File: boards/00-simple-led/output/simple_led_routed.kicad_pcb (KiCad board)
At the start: 2 copper layers, 25 x 20 mm, 3 parts, among them J1 PWR

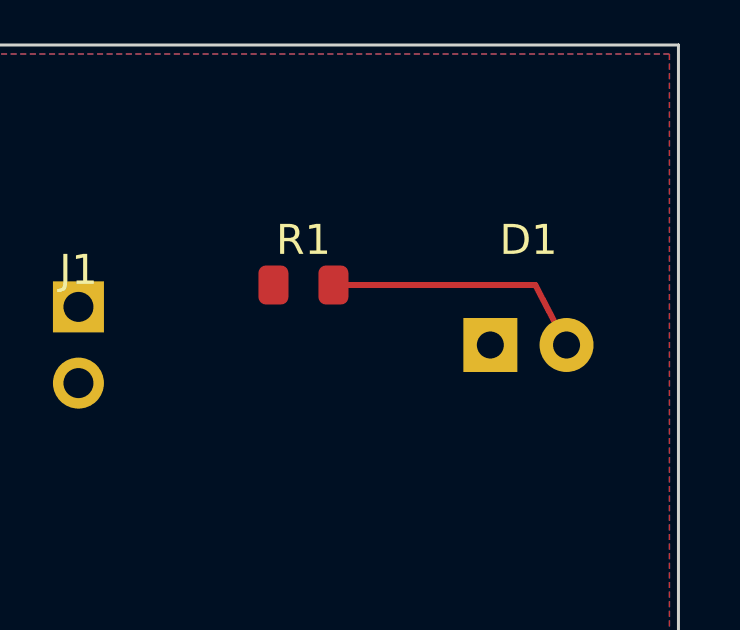
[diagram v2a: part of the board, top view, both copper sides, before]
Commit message: fix(board-00): true-45 LED_ANODE knee so the descent clears the 45° census gate
The GND-clearance guard in _rewrite_led_anode_route() nudged the knee to
(d1_gnd_x + 1.5, ...), giving the descent leg unequal dx/dy (1.04/2.0) =
62.53°, which fails the #3532 45°-alignment census gate
(test_fleet_45_census). Replace the off-45 nudge with a true-45 knee
(dx == dy, placed abs(dy) west of the anode); since the diagonal runs
south-east toward the anode it moves away from D1's GND pad (1.8mm
clearance), so no nudge is needed. Keep a 45-preserving safety fallback
(due-north 90° descent) for future footprint changes — never an off-45
nudge. Regenerate routed PCB + jlcpcb-tier1 manufacturing bundle.

Board 00 stays 0 under both DRC engines, LED_ANODE still connects
R1.2 → D1.2 (ANODE, not GND), diff is board-local.

Co-Authored-By: Claude Opus 4.7 <noreply@anthropic.com>
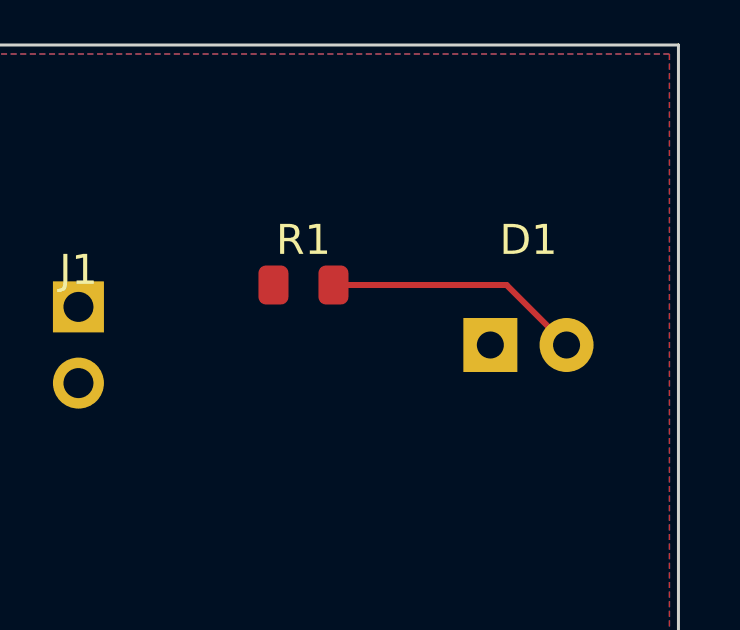
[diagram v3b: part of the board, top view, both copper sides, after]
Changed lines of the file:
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@@
 	(net 2 "LED_ANODE")
 	(net 3 "GND")
+	(footprint "Connector_PinHeader_2.54mm:PinHeader_1x02_P2.54mm_Vertical"
+		(layer "F.Cu")
+		(at 105 110)
+		(property "Reference" "J1"
+			(at 0 -2.5 0)
+			(layer "F.SilkS")
+			(effects
+				(font
+					(size 1 1)
+					(thickness 0.15)
+				)
+			)
+		)
+		(property "Value" "PWR"
+			(at 0 4 0)
+			(layer "F.Fab")
+			(effects
+				(font
+					(size 1 1)
+					(thickness 0.15)
+				)
+			)
+		)
+		(property "Datasheet" ""
+			(at 0 0 0)
+			(layer "F.Fab")
+			(hide yes)
+			(effects
+				(font
+					(size 1.27 1.27)
+				)
+			)
+		)
+		(property "Description" ""
+			(at 0 0 0)
+			(layer "F.Fab")
+			(hide yes)
+			(effects
+				(font
+					(size 1.27 1.27)
+				)
+			)
+		)
+		(duplicate_pad_numbers_are_jumpers no)
+		(pad "1" thru_hole rect
+			(at 0 -1.27)
+			(size 1.7 1.7)
+			(drill 1)
+			(layers "*.Cu" "*.Mask")
+			(remove_unused_layers no)
+			(net 1 "VCC")
+		)
+		(pad "2" thru_hole oval
+			(at 0 1.27)
+			(size 1.7 1.7)
+			(drill 1)
+			(layers "*.Cu" "*.Mask")
+			(remove_unused_layers no)
+			(net 3 "GND")
+		)
+		(embedded_fonts no)
+	)
+	(footprint "LED_THT:LED_D5.0mm"
+		(layer "F.Cu")
+		(at 120 110)
+		(property "Reference" "D1"
+			(at 0 -3.5 0)
+			(layer "F.SilkS")
+			(effects
+				(font
+					(size 1 1)
+					(thickness 0.15)
+				)
+			)
+		)
+		(property "Value" "LED"
+			(at 0 3.5 0)
+			(layer "F.Fab")
+			(effects
+				(font
+					(size 1 1)
+					(thickness 0.15)
+				)
+			)
+		)
+		(property "Datasheet" ""
+			(at 0 0 0)
+			(layer "F.Fab")
+			(hide yes)
+			(effects
+				(font
+					(size 1.27 1.27)
+				)
+			)
+		)
+		(property "Description" ""
+			(at 0 0 0)
+			(layer "F.Fab")
+			(hide yes)
+			(effects
+				(font
+					(size 1.27 1.27)
+				)
+			)
+		)
+		(duplicate_pad_numbers_are_jumpers no)
+		(pad "1" thru_hole rect
+			(at -1.27 0)
+			(size 1.8 1.8)
+			(drill 0.9)
+			(layers "*.Cu" "*.Mask")
+			(remove_unused_layers no)
+			(net 3 "GND")
+		)
+		(pad "2" thru_hole circle
+			(at 1.27 0)
+			(size 1.8 1.8)
+			(drill 0.9)
+			(layers "*.Cu" "*.Mask")
+			(remove_unused_layers no)
+			(net 2 "LED_ANODE")
+		)
+		(embedded_fonts no)
+	)
 	(footprint "Resistor_SMD:R_0805_2012Metric"
 		(layer "F.Cu")
@@
 		(embedded_fonts no)
 	)
-	(footprint "Connector_PinHeader_2.54mm:PinHeader_1x02_P2.54mm_Vertical"
-		(layer "F.Cu")
-		(at 105 110)
-		(property "Reference" "J1"
-			(at 0 -2.5 0)
-			(layer "F.SilkS")
-			(effects
-				(font
-					(size 1 1)
-					(thickness 0.15)
-				)
-			)
-		)
-		(property "Value" "PWR"
-			(at 0 4 0)
-			(layer "F.Fab")
-			(effects
-				(font
-					(size 1 1)
-					(thickness 0.15)
-				)
-			)
-		)
-		(property "Datasheet" ""
-			(at 0 0 0)
-			(layer "F.Fab")
-			(hide yes)
-			(effects
-				(font
-					(size 1.27 1.27)
-				)
-			)
-		)
-		(property "Description" ""
-			(at 0 0 0)
-			(layer "F.Fab")
-			(hide yes)
-			(effects
-				(font
-					(size 1.27 1.27)
-				)
-			)
-		)
-		(duplicate_pad_numbers_are_jumpers no)
-		(pad "1" thru_hole rect
-			(at 0 -1.27)
-			(size 1.7 1.7)
-			(drill 1)
-			(layers "*.Cu" "*.Mask")
-			(remove_unused_layers no)
-			(net 1 "VCC")
-		)
-		(pad "2" thru_hole oval
-			(at 0 1.27)
-			(size 1.7 1.7)
-			(drill 1)
-			(layers "*.Cu" "*.Mask")
-			(remove_unused_layers no)
-			(net 3 "GND")
-		)
-		(embedded_fonts no)
-	)
-	(footprint "LED_THT:LED_D5.0mm"
-		(layer "F.Cu")
-		(at 120 110)
-		(property "Reference" "D1"
-			(at 0 -3.5 0)
-			(layer "F.SilkS")
-			(effects
-				(font
-					(size 1 1)
-					(thickness 0.15)
-				)
-			)
-		)
-		(property "Value" "LED"
-			(at 0 3.5 0)
-			(layer "F.Fab")
-			(effects
-				(font
-					(size 1 1)
-					(thickness 0.15)
-				)
-			)
-		)
-		(property "Datasheet" ""
-			(at 0 0 0)
-			(layer "F.Fab")
-			(hide yes)
-			(effects
-				(font
-					(size 1.27 1.27)
-				)
-			)
-		)
-		(property "Description" ""
-			(at 0 0 0)
-			(layer "F.Fab")
-			(hide yes)
-			(effects
-				(font
-					(size 1.27 1.27)
-				)
-			)
-		)
-		(duplicate_pad_numbers_are_jumpers no)
-		(pad "1" thru_hole rect
-			(at -1.27 0)
-			(size 1.8 1.8)
-			(drill 0.9)
-			(layers "*.Cu" "*.Mask")
-			(remove_unused_layers no)
-			(net 3 "GND")
-		)
-		(pad "2" thru_hole circle
-			(at 1.27 0)
-			(size 1.8 1.8)
-			(drill 0.9)
-			(layers "*.Cu" "*.Mask")
-			(remove_unused_layers no)
-			(net 2 "LED_ANODE")
-		)
-		(embedded_fonts no)
-	)
 	(gr_rect
 		(start 100 100)
@@
 	)
 	(segment
-		(start 120.23 108)
+		(start 113.5 108)
+		(end 119.27 108)
+		(width 0.2)
+		(layer "F.Cu")
+		(net 2)
+	)
+	(segment
+		(start 119.27 108)
 		(end 121.27 110)
 		(width 0.2)
 		(layer "F.Cu")
-		(net 2)
-	)
-	(segment
-		(start 113.5 108)
-		(end 120.23 108)
-		(width 0.2)
-		(layer "F.Cu")

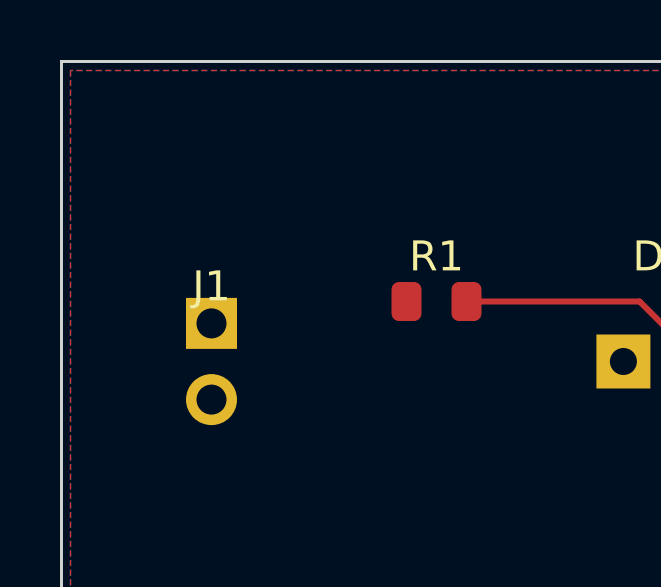
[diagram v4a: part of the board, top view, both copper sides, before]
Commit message: fix(boards): move connector refdes off pad-1 copper on boards 00/01 (#3962)
* fix(boards): move connector refdes off pad-1 copper on boards 00/01

The demo-board PCB generators for boards 00 (simple-led) and 01
(voltage-divider) hard-coded the connector refdes at local (0, -2.5),
placing the reference-designator text box over pad 1's exposed mask
aperture. Pad 1 is a 1.7x1.7 mm thru-hole centred at (0, -1.27), so its
copper top edge is at -2.12 mm; a 1x1 mm / 0.15 mm-stroke refdes has its
bottom edge 0.575 mm below centre, so -2.5 left the box inside the
aperture and fired silk_over_copper on J1/J2.

Move the connector refdes to (0, -3.5) -- the same offset the LED
footprint already uses and passes silk_over_copper -- which clears the
aperture with margin. Add a geometry-based justification in each
generate_connector docstring. The resistor refdes at (0, -1.5) was
already clear of the 0805 pads and is unchanged.

Regenerate boards 00 and 01 committed artifacts from the fixed
generators. Fresh kct check and kicad-cli pcb drc --refill-zones both
report 0 silk_over_copper (and 0 total DRC violations) on the routed
PCBs.

Remove the _SILK_PLACEMENT_RULES carve-out from
tests/test_board_01_ship_ready.py so the strict 0-warning gate holds
unconditionally, and move board 01 from the silk_over_copper positive
fixture to the clean-board list in tests/test_validate_silkscreen.py.

Closes #3939

Co-Authored-By: Claude Fable 5 <noreply@anthropic.com>

* fix(board-01): restore #3715 page-fit on regenerated routed artifact

The generator-only regen dropped the PAGE_FIT post-pass that produced
main's committed truth, reverting (paper "User" 40 35) -> (paper "A4")
and un-centering the board from ~10-30mm back to a full-A4 ~105-125mm
layout, silently undoing the #3715 gallery-centering.

Re-ran the routed artifact through the same pipeline main uses:
`kct pcb page-fit --margin 5.0` after routing, then regenerated the
JLCPCB manufacturing bundle from the page-fit board.

Verification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
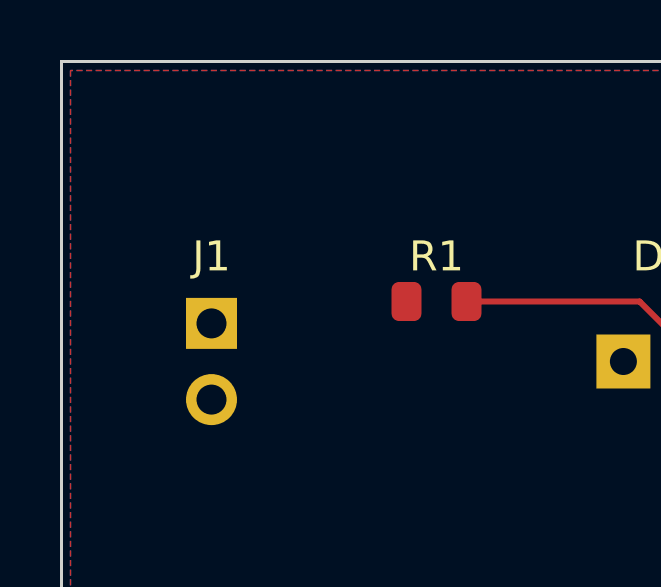
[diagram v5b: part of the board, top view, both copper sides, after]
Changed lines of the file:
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@@
+		(embedded_fonts no)
+	)
+	(footprint "Connector_PinHeader_2.54mm:PinHeader_1x02_P2.54mm_Vertical"
+		(layer "F.Cu")
+		(at 105 110)
+		(property "Reference" "J1"
+			(at 0 -3.5 0)
+			(layer "F.SilkS")
+			(effects
+				(font
+					(size 1 1)
+					(thickness 0.15)
+				)
+			)
+		)
+		(property "Value" "PWR"
+			(at 0 4 0)
+			(layer "F.Fab")
+			(effects
+				(font
+					(size 1 1)
+					(thickness 0.15)
+				)
+			)
+		)
+		(property "Datasheet" ""
+			(at 0 0 0)
+			(layer "F.Fab")
+			(hide yes)
+			(effects
+				(font
+					(size 1.27 1.27)
+				)
+			)
+		)
+		(property "Description" ""
+			(at 0 0 0)
+			(layer "F.Fab")
+			(hide yes)
+			(effects
+				(font
+					(size 1.27 1.27)
+				)
+			)
+		)
+		(duplicate_pad_numbers_are_jumpers no)
+		(pad "1" thru_hole rect
+			(at 0 -1.27)
+			(size 1.7 1.7)
+			(drill 1)
+			(layers "*.Cu" "*.Mask")
+			(remove_unused_layers no)
+			(net 1 "VCC")
+		)
+		(pad "2" thru_hole oval
+			(at 0 1.27)
+			(size 1.7 1.7)
+			(drill 1)
+			(layers "*.Cu" "*.Mask")
+			(remove_unused_layers no)
+			(net 3 "GND")
+		)
 		(embedded_fonts no)
 	)
@@
 		(embedded_fonts no)
 	)
-	(footprint "Connector_PinHeader_2.54mm:PinHeader_1x02_P2.54mm_Vertical"
-		(layer "F.Cu")
-		(at 105 110)
-		(property "Reference" "J1"
-			(at 0 -2.5 0)
-			(layer "F.SilkS")
-			(effects
-				(font
-					(size 1 1)
-					(thickness 0.15)
-				)
-			)
-		)
-		(property "Value" "PWR"
-			(at 0 4 0)
-			(layer "F.Fab")
-			(effects
-				(font
-					(size 1 1)
-					(thickness 0.15)
-				)
-			)
-		)
-		(property "Datasheet" ""
-			(at 0 0 0)
-			(layer "F.Fab")
-			(hide yes)
-			(effects
-				(font
-					(size 1.27 1.27)
-				)
-			)
-		)
-		(property "Description" ""
-			(at 0 0 0)
-			(layer "F.Fab")
-			(hide yes)
-			(effects
-				(font
-					(size 1.27 1.27)
-				)
-			)
-		)
-		(duplicate_pad_numbers_are_jumpers no)
-		(pad "1" thru_hole rect
-			(at 0 -1.27)
-			(size 1.7 1.7)
-			(drill 1)
-			(layers "*.Cu" "*.Mask")
-			(remove_unused_layers no)
-			(net 1 "VCC")
-		)
-		(pad "2" thru_hole oval
-			(at 0 1.27)
-			(size 1.7 1.7)
-			(drill 1)
-			(layers "*.Cu" "*.Mask")
-			(remove_unused_layers no)
-			(net 3 "GND")
-		)
-		(embedded_fonts no)
-	)
 	(gr_rect
 		(start 100 100)
@@
 	)
 	(segment
-		(start 113.5 108)
-		(end 119.27 108)
+		(start 119.27 108)
+		(end 121.27 110)
 		(width 0.2)
 		(layer "F.Cu")
@@
 	)
 	(segment
-		(start 119.27 108)
-		(end 121.27 110)
+		(start 113.5 108)
+		(end 119.27 108)
 		(width 0.2)
 		(layer "F.Cu")
